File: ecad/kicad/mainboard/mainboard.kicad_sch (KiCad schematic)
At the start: 34 parts, among them IC1 74HC86, J1 SENSORS, J2 CONN_06SILK_FEMALE_PTH, J3 CONN_06SILK_FEMALE_PTH, J4 POWER, J5 SERIAL, M1 Left Motor, M2 Right Motor, U1 Arduino_Nano, U2 TB6612FNG-Module

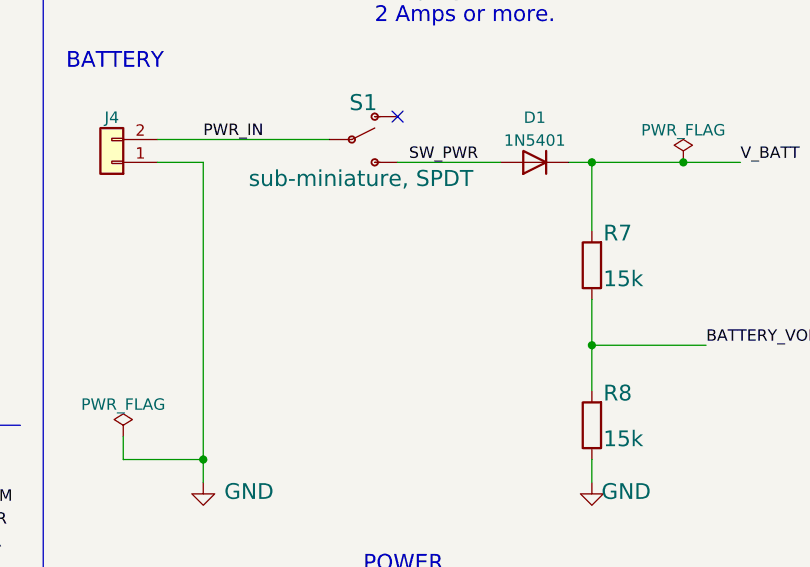
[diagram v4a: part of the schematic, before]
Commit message: use new switch footprint on V1.3 board
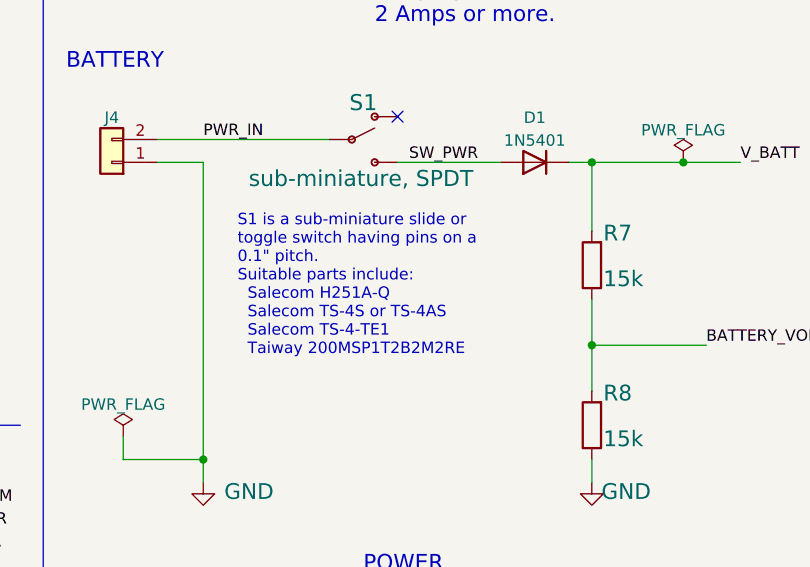
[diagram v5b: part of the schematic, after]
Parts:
- S1: footprint ukmarsbot:SW_MINI_SPDT_TOGGLE_DAILYWELL_FS1S102M2QES -> ukmarsbot:SW_MINI-SPDT-RTECH-78-0564
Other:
- note added: "S1 is a sub-miniature slide or toggle switch having pins on a 0.1" pitch. Suitable parts include: Salecom H251A-Q Salecom TS-4S or TS-4AS Salecom TS-4-TE1 Taiway 200MSP1T2B2M2RE"
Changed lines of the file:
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@@
+    (effects (font (size 1.27 1.27)) (justify left bottom))
+  )
+  (text "S1 is a sub-miniature slide or\ntoggle switch having pins on a \n0.1\" pitch.\nSuitable parts include:\n  Salecom H251A-Q\n  Salecom TS-4S or TS-4AS\n  Salecom TS-4-TE1\n  Taiway 200MSP1T2B2M2RE"
+    (at 214.63 58.42 0)
     (effects (font (size 1.27 1.27)) (justify left bottom))
   )
@@
       (effects (font (size 1.778 1.778)) (justify top))
     )
-    (property "Footprint" "ukmarsbot:SW_MINI_SPDT_TOGGLE_DAILYWELL_FS1S102M2QES" (id 2) (at 227.33 34.29 0)
+    (property "Footprint" "ukmarsbot:SW_MINI-SPDT-RTECH-78-0564" (id 2) (at 227.33 34.29 0)
       (effects (font (size 1.27 1.27)) hide)
     )
@@
     )
     (path "/e3713f85-2a22-40fc-8498-9a1d5ba496c5"
-      (reference "S1") (unit 1) (value "sub-miniature, SPDT") (footprint "ukmarsbot:SW_MINI_SPDT_TOGGLE_DAILYWELL_FS1S102M2QES")
+      (reference "S1") (unit 1) (value "sub-miniature, SPDT") (footprint "ukmarsbot:SW_MINI-SPDT-RTECH-78-0564")
     )
     (path "/d0feb225-71a8-4533-9b0a-f0eabf97a0e5"
